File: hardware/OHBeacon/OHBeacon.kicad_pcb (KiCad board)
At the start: 2 copper layers, 100 x 100 mm, 57 parts, among them J1 Conn_01x04_Socket, J2 Conn_01x01_Pin, J3 Conn_01x01_Pin, J4 USB_C_Receptacle_PowerOnly_6P, J5 Conn_01x01_Pin, J6 Conn_01x01_Pin, J7 Conn_01x02_Pin, Q1 DMG2305UX-7, SW1 SW_Push, SW2 SW_Push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

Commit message: prelim beacon pcb
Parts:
- removed SW1, SW2: SW_Push, Button_Switch_THT:SW_PUSH_6mm
- added BOOT: SW_Push, Button_Switch_THT:SW_PUSH_6mm, F.Cu at (110.5, 90.0)
- added EN: SW_Push, Button_Switch_THT:SW_PUSH_6mm, F.Cu at (96.0, 90.0)
- added R10: 100k, Resistor_SMD:R_0603_1608Metric, F.Cu at (95.0, 134.5)
- added R11: 0, Resistor_SMD:R_0603_1608Metric, F.Cu at (106.0, 113.0)
- moved J3 117.3 mm to (54.2, 54.0)
- moved C8 115.2 mm to (60.0, 125.5)
- moved D8 115.1 mm to (60.0, 120.0)
- moved J5 113.5 mm to (145.8, 54.0)
- moved D6 106.0 mm to (70.0, 140.0)
- moved C6 101.6 mm to (70.0, 134.8)
- moved J2 95.4 mm to (54.2, 146.0)
- moved D10 88.9 mm to (60.0, 80.0)
- moved C10 88.8 mm to (60.0, 85.5)
- moved D4 88.4 mm to (80.0, 110.0)
- moved C4 88.2 mm to (80.0, 115.5)
- moved J1 86.5 mm to (112.5, 61.2), turned to 0 degrees
- moved D2 82.5 mm to (80.0, 90.0)
- moved C2 82.3 mm to (80.0, 95.5)
- moved C12 78.2 mm to (70.0, 65.5)
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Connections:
- U2 pad 12: unconnected-(U2-ILIM-Pad12) -> Net-(U2-ILIM)
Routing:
- net Net-(J5-Pin_1): track 0.00 -> 114.9 mm, vias 0 -> 1
- net Net-(J3-Pin_1): track 0.00 -> 113.5 mm, vias 0 -> 1
- net +5V: track 0.00 -> 89.0 mm
- net Net-(D10-DIN): track 0.00 -> 46.3 mm
- net GND: track 0.00 -> 44.8 mm, vias 0 -> 45
- net +BATT: track 0.00 -> 42.5 mm, vias 0 -> 3
- net Net-(D3-DOUT): track 0.00 -> 38.7 mm
- net /DCON: track 0.00 -> 36.5 mm
- net Net-(D7-DOUT): track 0.00 -> 35.4 mm
- net /IO9: track 0.00 -> 34.2 mm, vias 0 -> 2
- net /EN: track 0.00 -> 34.0 mm
- net Net-(J6-Pin_1): track 0.00 -> 31.0 mm, vias 0 -> 1
- net Net-(D10-DOUT): track 0.00 -> 29.5 mm
- net Net-(D4-DOUT): track 0.00 -> 28.8 mm
- net Net-(J2-Pin_1): track 0.00 -> 28.5 mm, vias 0 -> 1
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- added copper zone on F.Cu, net +3.3V
- added copper zone on B.Cu, net GND
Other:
- outline, holes or cut-outs redrawn

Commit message: Changed some stuff in the schematic :)
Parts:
- added C21: 1.0uF, Capacitor_SMD:C_0603_1608Metric, F.Cu at (101.2, 138.2)
- renumbered EN to SW1, BOOT to SW2
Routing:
- net GND: track 44.8 -> 52.6 mm, vias 45 -> 50
- net +3.3V: track 0.00 -> 4.24 mm
- net Net-(D10-DIN): track 46.3 -> 47.1 mm
- net +BATT: track 42.5 -> 43.3 mm, vias 3 -> 5
- net Net-(D7-DOUT): track 35.4 -> 36.0 mm
- net Net-(D1-DOUT): track 24.0 -> 24.5 mm

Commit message: updated beacon
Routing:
- net /IO9: track 34.2 -> 40.7 mm
- net /EN: track 34.0 -> 40.5 mm
- net /DIN: track 25.2 -> 27.2 mm
- net GND: track 52.6 -> 53.4 mm, vias 50 -> 51
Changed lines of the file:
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@@
+	)
+	(segment
+		(start 97.25 144.264918)
+		(end 96.992541 144.007459)
+		(width 0.75)
+		(layer "F.Cu")
+		(net 2)
 	)
 	(segment
@@
 		(end 131.1 61.65)
 		(width 0.5)
+		(layer "F.Cu")
+		(net 2)
+	)
+	(segment
+		(start 97.25 144.75)
+		(end 97.25 144.264918)
+		(width 0.75)
 		(layer "F.Cu")
 		(net 2)
@@
 	)
 	(via
+		(at 96.992541 144.007459)
+		(size 0.6)
+		(drill 0.3)
+		(layers "F.Cu" "B.Cu")
+		(net 2)
+	)
+	(via
 		(at 71.5 65.5)
 		(size 0.6)
@@
 	)
 	(segment
+		(start 89.5 85.5)
+		(end 96 85.5)
+		(width 0.2)
+		(layer "F.Cu")
+		(net 3)
+	)
+	(segment
 		(start 96.9 81.75)
 		(end 96.9 63.55)
@@
 	)
 	(segment
+		(start 104 85.5)
+		(end 110.5 85.5)
+		(width 0.2)
+		(layer "F.Cu")
+		(net 4)
+	)
+	(segment
 		(start 94.4 67.85)
 		(end 94.5 67.75)
@@
 	)
 	(segment
-		(start 111.068 60)
-		(end 111.199 60)
+		(start 131.35 57.25)
+		(end 132.45 58.35)
 		(width 0.5)
 		(layer "F.Cu")
@@
 	)
 	(segment
-		(start 111.199 59.869)
-		(end 130.931 59.869)
+		(start 112 57.25)
+		(end 110.25 59)
 		(width 0.5)
 		(layer "F.Cu")
@@
 	)
 	(segment
-		(start 111.199 60)
-		(end 111.199 59.869)
+		(start 108.75 61.85)
+		(end 109.352 61.85)
 		(width 0.5)
 		(layer "F.Cu")
@@
 	)
 	(segment
-		(start 108.75 61.85)
-		(end 109.218 61.85)
+		(start 109.352 61.85)
+		(end 110.25 60.952)
 		(width 0.5)
 		(layer "F.Cu")
@@
 	)
 	(segment
-		(start 130.931 59.869)
-		(end 132.45 58.35)
+		(start 110.25 59)
+		(end 110.25 60.952)
 		(width 0.5)
 		(layer "F.Cu")
@@
 	)
 	(segment
-		(start 109.218 61.85)
-		(end 111.068 60)
-		(width 0.5)
-		(layer "F.Cu")
+		(start 131.35 57.25)
+		(end 112 57.25)
+		(width 0.5)
+		(layer "F.Cu")

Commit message: okay it's fine for prod ig
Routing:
- net +3.3V: track 4.24 -> 0.00 mm
- net +BATT: track 43.3 -> 42.3 mm, vias 5 -> 4
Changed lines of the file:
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@@
-	)
-	(segment
-		(start 88 59.75)
-		(end 90.4 57.35)
-		(width 0.5)
-		(layer "F.Cu")
-		(net 1)
-	)
-	(segment
-		(start 90.4 57.35)
-		(end 91.25 57.35)
-		(width 0.5)
-		(layer "F.Cu")
-		(net 1)
 	)
 	(segment
@@
 	)
 	(segment
-		(start 98.5625 115.75)
-		(end 96 115.75)
-		(width 0.25)
+		(start 96.125 115.875)
+		(end 98.4375 115.875)
+		(width 0.2)
 		(layer "F.Cu")
 		(net 2)
@@
 	)
 	(segment
+		(start 98.4375 115.875)
+		(end 98.5625 115.75)
+		(width 0.2)
+		(layer "F.Cu")
+		(net 2)
+	)
+	(segment
 		(start 120.75 95.5)
 		(end 122.05 95.5)
@@
 		(end 91.43 81.75)
 		(width 0.5)
+		(layer "F.Cu")
+		(net 2)
+	)
+	(segment
+		(start 96 115.75)
+		(end 96.125 115.875)
+		(width 0.2)
 		(layer "F.Cu")
 		(net 2)
@@
 	(via
 		(at 97.33 115.12)
-		(size 0.6)
-		(drill 0.3)
-		(layers "F.Cu" "B.Cu")
-		(net 41)
-	)
-	(via
-		(at 96.5575 114.7825)
-		(size 0.6)
-		(drill 0.3)
+		(size 0.9)
+		(drill 0.6)
 		(layers "F.Cu" "B.Cu")
 		(net 41)
@@
 	)
 	(segment
-		(start 96.97 114.76)
-		(end 97.33 115.12)
-		(width 1)
-		(layer "B.Cu")
-		(net 41)
-	)
-	(segment
 		(start 97.33 115.12)
 		(end 103.21 121)
 		(width 1)
 		(layer "B.Cu")
-		(net 41)
-	)
-	(segment
-		(start 96.54 114.76)
-		(end 96.97 114.76)
-		(width 1)
-		(layer "B.Cu")

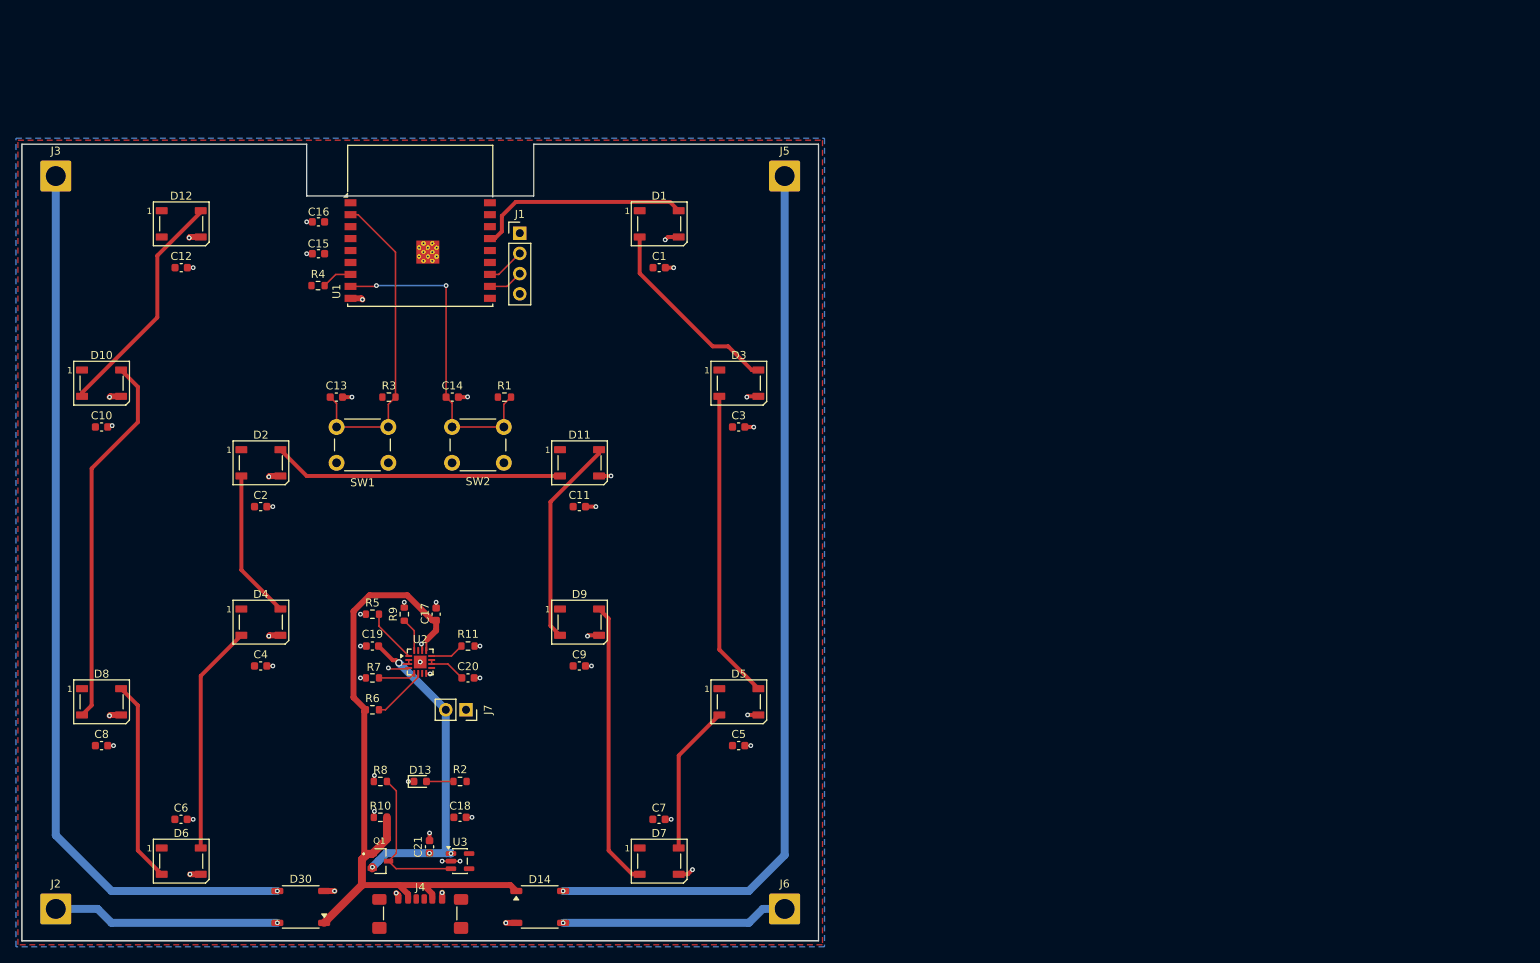
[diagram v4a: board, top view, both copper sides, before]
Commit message: new oh beacon schematic and early routing
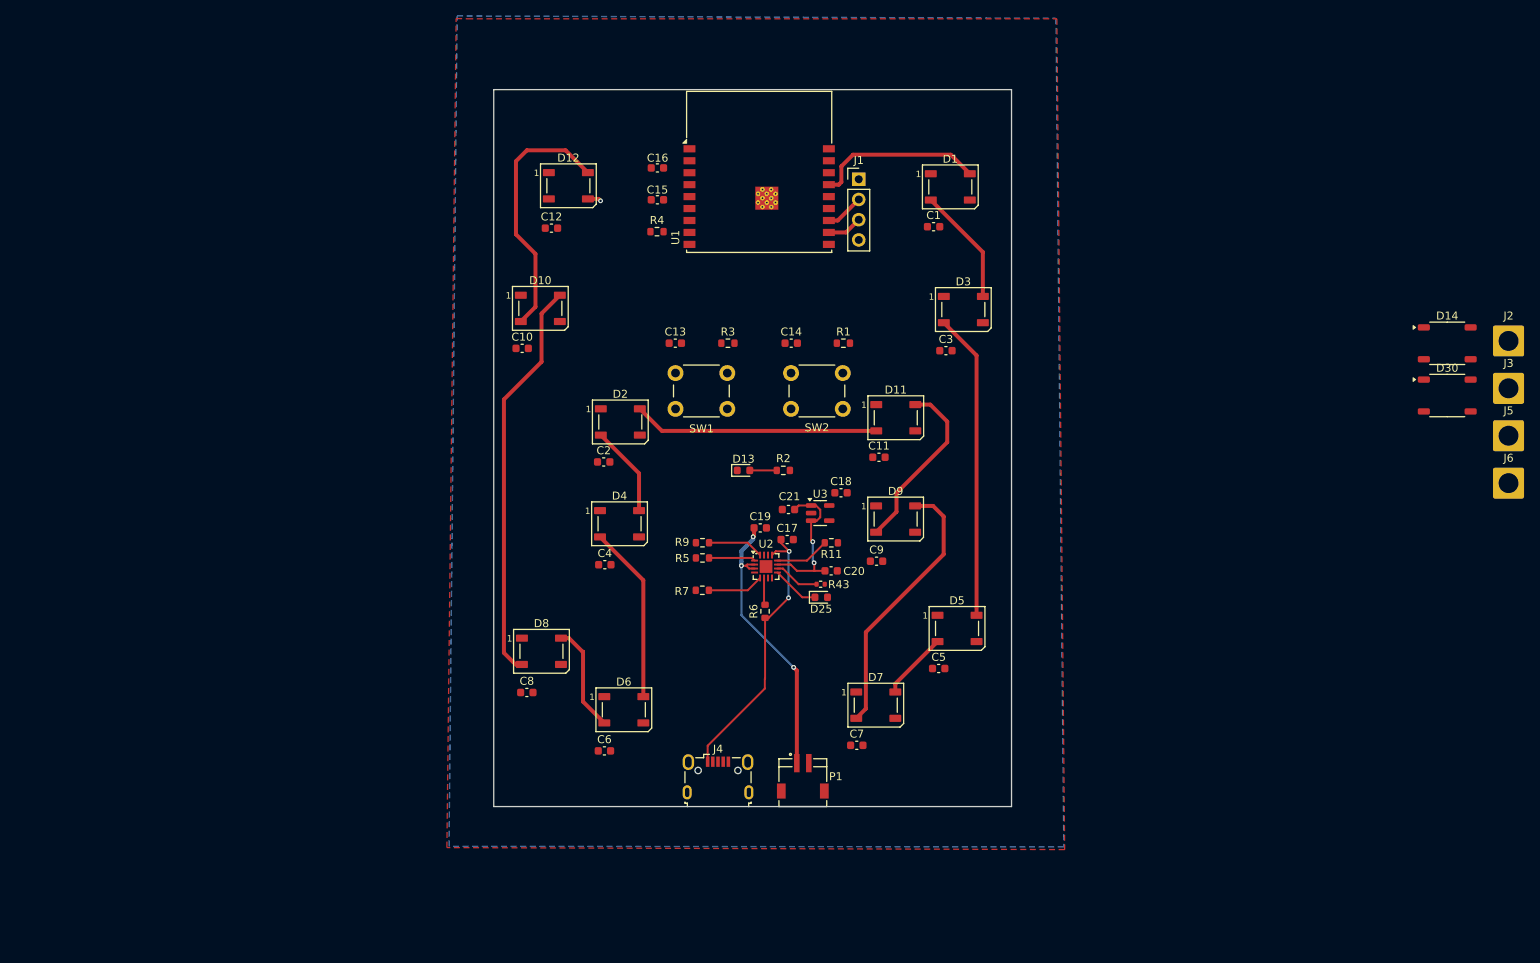
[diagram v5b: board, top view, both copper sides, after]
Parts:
- removed J7: Conn_01x02_Pin, Connector_PinSocket_2.54mm:PinSocket_1x02_P2.54mm_Vertical
- removed Q1: DMG2305UX-7, DMG2305UX-7:SOT91P240X110-3N_DMG2305UX-7
- removed R10, R8: 100k, Resistor_SMD:R_0603_1608Metric
- added D25: GREEN, LED_SMD:LED_0603_1608Metric, F.Cu at (150.3, 106.9)
- added P1: S2B-ZR-SM4A-TF, custom footprints:JST_S2B-ZR-SM4A-TF, F.Cu at (148.0, 127.7)
- added R43: 1k5, Resistor_SMD:R_0402_1005Metric, F.Cu at (150.3, 105.2)
- J4: value USB_C_Receptacle_PowerOnly_6P -> USB_B_Micro; footprint Connector_USB:USB_C_Receptacle_GCT_USB4135-GF-A_6P_TopMnt_Horizontal -> Connector_USB:USB_Micro-B_Wuerth_629105150521
- moved J2 195.8 mm to (236.6, 74.7)
- moved J3 184.3 mm to (236.6, 80.7)
- moved D30 157.6 mm to (228.9, 81.5), turned to 0 degrees
- moved D14 134.1 mm to (228.9, 75.0)
- moved J6 105.4 mm to (236.6, 92.5)
- moved J5 96.5 mm to (236.6, 86.6)
- moved U3 62.9 mm to (150.2, 96.3)
- moved C18 62.8 mm to (152.8, 93.8)
- moved C21 61.8 mm to (146.2, 95.9), turned to 180 degrees
- moved D6 58.7 mm to (125.6, 121.0)
- moved D13 56.3 mm to (140.6, 91.0)
- moved R2 56.3 mm to (145.6, 91.0)
- moved D10 55.9 mm to (115.1, 70.6)
- moved D8 55.6 mm to (115.2, 113.7)
- moved C6 53.8 mm to (123.1, 126.2)
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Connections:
- C20 pad 1: Net-(C20-Pad1) -> Net-(U3-EN)
- C21 pad 1: +BATT -> Net-(U3-EN)
- U2 pad 10: Net-(C20-Pad1) -> Net-(U3-EN)
- U2 pad 11: Net-(C20-Pad1) -> Net-(U3-EN)
- U2 pad 9: unconnected-(U2-~{CHG}-Pad9) -> Net-(D25-K)
- U3 pad 1: +BATT -> Net-(U3-EN)
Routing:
- net Net-(J5-Pin_1): track 114.9 -> 0.00 mm, vias 1 -> 0
- net Net-(J3-Pin_1): track 113.5 -> 0.00 mm, vias 1 -> 0
- net +5V: track 89.1 -> 35.2 mm, vias 0 -> 2
- net GND: track 53.5 -> 1.69 mm, vias 51 -> 1
- net /IO9: track 40.7 -> 0.00 mm, vias 2 -> 0
- net /EN: track 40.5 -> 0.00 mm
- net Net-(J6-Pin_1): track 31.0 -> 0.00 mm, vias 1 -> 0
- net Net-(J2-Pin_1): track 28.5 -> 0.00 mm, vias 1 -> 0
- net Net-(D6-DOUT): track 25.4 -> 13.5 mm
- net Net-(D5-DOUT): track 18.8 -> 8.53 mm
- net Net-(D1-DOUT): track 24.5 -> 14.8 mm
- net Net-(D2-DOUT): track 18.7 -> 11.5 mm
- net Net-(D4-DOUT): track 28.8 -> 22.3 mm
- net +BATT: track 42.3 -> 36.0 mm, vias 4 -> 3
- net Net-(D25-K): track 0.00 -> 5.99 mm
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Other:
- board size 100 x 100 mm -> 65 x 90 mm

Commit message: fml
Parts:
- removed C18, C21: 1.0uF, Capacitor_SMD:C_0603_1608Metric
- removed C19, C20: 4.7uF, Capacitor_SMD:C_0603_1608Metric
- removed D11, D12: WS2812B, LED_SMD:LED_WS2812B_PLCC4_5.0x5.0mm_P3.2mm
- removed D13: LED, LED_SMD:LED_0603_1608Metric
- removed D14, D30: MDB6S, Package_SO:TSSOP-4_4.4x5mm_P4mm
- removed D25: GREEN, LED_SMD:LED_0603_1608Metric
- removed R11: 0, Resistor_SMD:R_0603_1608Metric
- removed R43: 1k5, Resistor_SMD:R_0402_1005Metric
- added R10: 0, Resistor_SMD:R_0805_2012Metric_Pad1.20x1.40mm_HandSolder, F.Cu at (82.2, 99.5)
- added R8: 1k, Resistor_SMD:R_0805_2012Metric_Pad1.20x1.40mm_HandSolder, F.Cu at (101.5, 92.5)
- C1, C10, C11, C12, C2, C3, C4, C5, C6, C7, C8: footprint Capacitor_SMD:C_0603_1608Metric -> Capacitor_SMD:C_0805_2012Metric_Pad1.18x1.45mm_HandSolder
- C13, C14: value 0.1uF -> 4.7uF; footprint Capacitor_SMD:C_0603_1608Metric -> Capacitor_SMD:C_0805_2012Metric_Pad1.18x1.45mm_HandSolder
- C15: value 10uF -> 4.7uF; footprint Capacitor_SMD:C_0603_1608Metric -> Capacitor_SMD:C_0805_2012Metric_Pad1.18x1.45mm_HandSolder
- C16: value 0.1uF -> 1.0uF; footprint Capacitor_SMD:C_0603_1608Metric -> Capacitor_SMD:C_0805_2012Metric_Pad1.18x1.45mm_HandSolder
- C17: value 4.7uF -> 1.0uF; footprint Capacitor_SMD:C_0603_1608Metric -> Capacitor_SMD:C_0805_2012Metric_Pad1.18x1.45mm_HandSolder
- C9: value 0.1uF -> 10uF; footprint Capacitor_SMD:C_0603_1608Metric -> Capacitor_SMD:C_0805_2012Metric_Pad1.18x1.45mm_HandSolder
- D10: value WS2812B -> GREEN; footprint LED_SMD:LED_WS2812B_PLCC4_5.0x5.0mm_P3.2mm -> LED_SMD:LED_0805_2012Metric_Pad1.15x1.40mm_HandSolder
- D9: value WS2812B -> RED; footprint LED_SMD:LED_WS2812B_PLCC4_5.0x5.0mm_P3.2mm -> LED_SMD:LED_0805_2012Metric_Pad1.15x1.40mm_HandSolder
- J1: value Conn_01x04_Socket -> Conn_01x01_Pin; footprint Connector_PinHeader_2.54mm:PinHeader_1x04_P2.54mm_Vertical -> Connector_Wire:SolderWire-1sqmm_1x01_D1.4mm_OD3.9mm
- J2, J3: footprint Connector_Wire:SolderWire-2sqmm_1x01_D2mm_OD3.9mm -> Connector_Wire:SolderWire-1sqmm_1x01_D1.4mm_OD3.9mm
- J4: value USB_B_Micro -> Conn_01x01_Pin; footprint Connector_USB:USB_Micro-B_Wuerth_629105150521 -> Connector_Wire:SolderWire-1sqmm_1x01_D1.4mm_OD3.9mm
- J5: value Conn_01x01_Pin -> USB_B_Micro; footprint Connector_Wire:SolderWire-2sqmm_1x01_D2mm_OD3.9mm -> Connector_USB:USB_Micro-B_Wuerth_629105150521
- J6: value Conn_01x01_Pin -> Conn_01x04_Socket; footprint Connector_Wire:SolderWire-2sqmm_1x01_D2mm_OD3.9mm -> Connector_PinHeader_2.54mm:PinHeader_1x04_P2.54mm_Vertical
- R1: value 10k -> 1K; footprint Resistor_SMD:R_0603_1608Metric -> Resistor_SMD:R_0805_2012Metric_Pad1.20x1.40mm_HandSolder
- R2: value 150 -> 10k; footprint Resistor_SMD:R_0603_1608Metric -> Resistor_SMD:R_0805_2012Metric_Pad1.20x1.40mm_HandSolder
- R3, R4, R6: footprint Resistor_SMD:R_0603_1608Metric -> Resistor_SMD:R_0805_2012Metric_Pad1.20x1.40mm_HandSolder
- R5: value 10k -> 100k; footprint Resistor_SMD:R_0603_1608Metric -> Resistor_SMD:R_0805_2012Metric_Pad1.20x1.40mm_HandSolder
- R7: value 100k -> 1k; footprint Resistor_SMD:R_0603_1608Metric -> Resistor_SMD:R_0805_2012Metric_Pad1.20x1.40mm_HandSolder
- R9: value 1k -> 10k; footprint Resistor_SMD:R_0603_1608Metric -> Resistor_SMD:R_0805_2012Metric_Pad1.20x1.40mm_HandSolder
- SW1: value SW_Push -> EN
- SW2: value SW_Push -> I09
- moved J5 143.8 mm to (95.0, 111.2)
- moved J6 131.7 mm to (109.0, 60.0)
- moved D7 112.1 mm to (56.5, 71.2)
- moved C7 107.2 mm to (62.5, 71.0)
- moved J3 103.8 mm to (136.0, 106.0)
- moved P1 102.9 mm to (55.6, 82.5), turned to 90 degrees
- moved J2 102.7 mm to (136.0, 54.0)
- moved J1 101.1 mm to (54.0, 54.0)
- moved D5 98.7 mm to (69.0, 103.5)
- moved C5 89.9 mm to (76.0, 104.0)
- moved J4 86.6 mm to (54.0, 106.0)
- moved C9 85.8 mm to (80.7, 63.8)
- moved D6 75.7 mm to (55.5, 92.2)
- moved D8 74.7 mm to (67.2, 56.4)
- moved C8 74.0 mm to (73.5, 56.5)
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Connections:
- C11 pad 1: +3.3V -> /EN
- C12 pad 1: +3.3V -> /IO9
- C13 pad 1: /EN -> +BATT
- C14 pad 1: /IO9 -> Net-(U3-EN)
- C15 pad 1: +3.3V -> +5V
- C16 pad 1: +3.3V -> Net-(U3-EN)
- C17 pad 1: +5V -> +3.3V
- D10 pad 1: +3.3V -> Net-(D10-K)
- D2 pad 4: /DCON -> Net-(D1-DOUT)
- D3 pad 4: Net-(D1-DOUT) -> Net-(D2-DOUT)
- D4 pad 2: Net-(D4-DOUT) -> /DCON
- D4 pad 4: Net-(D2-DOUT) -> Net-(D3-DOUT)
- D5 pad 4: Net-(D3-DOUT) -> /DCON
- D6 pad 4: Net-(D4-DOUT) -> Net-(D5-DOUT)
- D7 pad 4: Net-(D5-DOUT) -> Net-(D6-DOUT)
- D8 pad 2: Net-(D10-DIN) -> unconnected-(D8-DOUT-Pad2)
- D8 pad 4: Net-(D6-DOUT) -> Net-(D7-DOUT)
- D9 pad 1: +3.3V -> GND
- D9 pad 2: Net-(D11-DIN) -> Net-(D9-A)
- J1 pad 1: +3.3V -> +5V
- J2 pad 1: Net-(J2-Pin_1) -> GND
- J3 pad 1: Net-(J3-Pin_1) -> +5V
- J4 pad 1: +5V -> GND
- J5 pad 1: Net-(J5-Pin_1) -> +5V
- J6 pad 1: Net-(J6-Pin_1) -> +3.3V
- R1 pad 2: /IO9 -> Net-(D9-A)
- R2 pad 2: Net-(D13-A) -> /EN
- R3 pad 2: /EN -> /IO9
- R5 pad 1: GND -> +5V
- R5 pad 2: Net-(U2-TS) -> Net-(U2-EN1)
- R6 pad 1: +5V -> GND
- R6 pad 2: Net-(U2-EN1) -> Net-(U2-EN2)
- R7 pad 2: Net-(U2-EN2) -> Net-(U2-ISET)
- R9 pad 2: Net-(U2-ISET) -> Net-(U2-TS)
- U2 pad 9: Net-(D25-K) -> Net-(D10-K)
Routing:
- net Net-(D10-DIN): track 50.7 -> 0.00 mm
- net Net-(D3-DOUT): track 38.4 -> 0.00 mm
- net +BATT: track 36.0 -> 0.00 mm, vias 3 -> 0
- net +5V: track 35.2 -> 0.00 mm, vias 2 -> 0
- net Net-(D7-DOUT): track 34.0 -> 0.00 mm
- net Net-(D10-A): track 32.7 -> 0.00 mm
- net /DCON: track 30.8 -> 0.00 mm
- net Net-(U3-EN): track 24.4 -> 0.00 mm, vias 2 -> 0
- net Net-(D11-DIN): track 22.5 -> 0.00 mm
- net Net-(D4-DOUT): track 22.3 -> 0.00 mm
- net /DIN: track 21.4 -> 0.00 mm
- net Net-(D1-DOUT): track 14.8 -> 0.00 mm
- net Net-(D6-DOUT): track 13.5 -> 0.00 mm
- net Net-(D2-DOUT): track 11.5 -> 0.00 mm
- net Net-(D5-DOUT): track 8.53 -> 0.00 mm
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- removed copper zone on F.Cu, net +3.3V
- removed copper zone on B.Cu, net GND
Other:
- board size 65 x 90 mm -> 90 x 65 mm

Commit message: new charging
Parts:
- removed C13, C14, C15: 4.7uF, Capacitor_SMD:C_0805_2012Metric_Pad1.18x1.45mm_HandSolder
- removed C16, C17: 1.0uF, Capacitor_SMD:C_0805_2012Metric_Pad1.18x1.45mm_HandSolder
- removed D10: GREEN, LED_SMD:LED_0805_2012Metric_Pad1.15x1.40mm_HandSolder
- removed D9: RED, LED_SMD:LED_0805_2012Metric_Pad1.15x1.40mm_HandSolder
- removed R1: 1K, Resistor_SMD:R_0805_2012Metric_Pad1.20x1.40mm_HandSolder
- removed R10: 0, Resistor_SMD:R_0805_2012Metric_Pad1.20x1.40mm_HandSolder
- removed R5, R6: 100k, Resistor_SMD:R_0805_2012Metric_Pad1.20x1.40mm_HandSolder
- removed R7, R8: 1k, Resistor_SMD:R_0805_2012Metric_Pad1.20x1.40mm_HandSolder
- removed R9: 10k, Resistor_SMD:R_0805_2012Metric_Pad1.20x1.40mm_HandSolder
- removed U2: BQ24074RGT, Package_DFN_QFN:VQFN-16-1EP_3x3mm_P0.5mm_EP1.6x1.6mm
- removed U3: AP2112K-3.3, Package_TO_SOT_SMD:SOT-23-5
- J5: value USB_B_Micro -> USB_C_Receptacle_PowerOnly_6P; footprint Connector_USB:USB_Micro-B_Wuerth_629105150521 -> Connector_USB:USB_C_Receptacle_GCT_USB4135-GF-A_6P_TopMnt_Horizontal
- P1: moved to B.Cu
- moved D6 24.5 mm to (78.0, 82.5)
- moved C3 23.2 mm to (112.0, 87.8)
- moved D2 19.6 mm to (112.0, 82.5)
- moved C7 17.6 mm to (57.0, 87.8)
- moved C6 16.5 mm to (78.0, 87.8)
- moved C2 15.8 mm to (133.0, 87.8)
- moved D7 11.3 mm to (57.0, 82.5)
- moved D4 9.02 mm to (121.2, 109.5)
- moved D3 7.91 mm to (133.0, 82.5)
- moved C5 7.22 mm to (68.8, 104.2)
- moved C8 6.35 mm to (68.8, 60.8)
- moved D5 6.01 mm to (68.8, 109.5)
- moved J3 5.00 mm to (136.0, 111.0)
- moved J4 5.00 mm to (54.0, 111.0)
- moved J5 2.16 mm to (96.2, 113.0)
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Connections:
- C1 pad 1: +3.3V -> +BATT
- C2 pad 1: +3.3V -> +BATT
- C3 pad 1: +3.3V -> +BATT
- C4 pad 1: +3.3V -> +BATT
- C5 pad 1: +3.3V -> +BATT
- C6 pad 1: +3.3V -> +BATT
- C7 pad 1: +3.3V -> +BATT
- C8 pad 1: +3.3V -> +BATT
- D1 pad 1: +3.3V -> +BATT
- D2 pad 1: +3.3V -> +BATT
- D3 pad 1: +3.3V -> +BATT
- D4 pad 1: +3.3V -> +BATT
- D5 pad 1: +3.3V -> +BATT
- D6 pad 1: +3.3V -> +BATT
- D7 pad 1: +3.3V -> +BATT
- D8 pad 1: +3.3V -> +BATT
